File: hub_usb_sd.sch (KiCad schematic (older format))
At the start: 65 parts, among them J1 Downstream_2, J2 Downstream_3, J3 I²C, J4 Upstream, J5 SD_Card, J6 EEPROM_Pgm, J7 External_Power, U1 USB2642-I_ML, U2 TPS2052C, U3 AT24CS04BN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

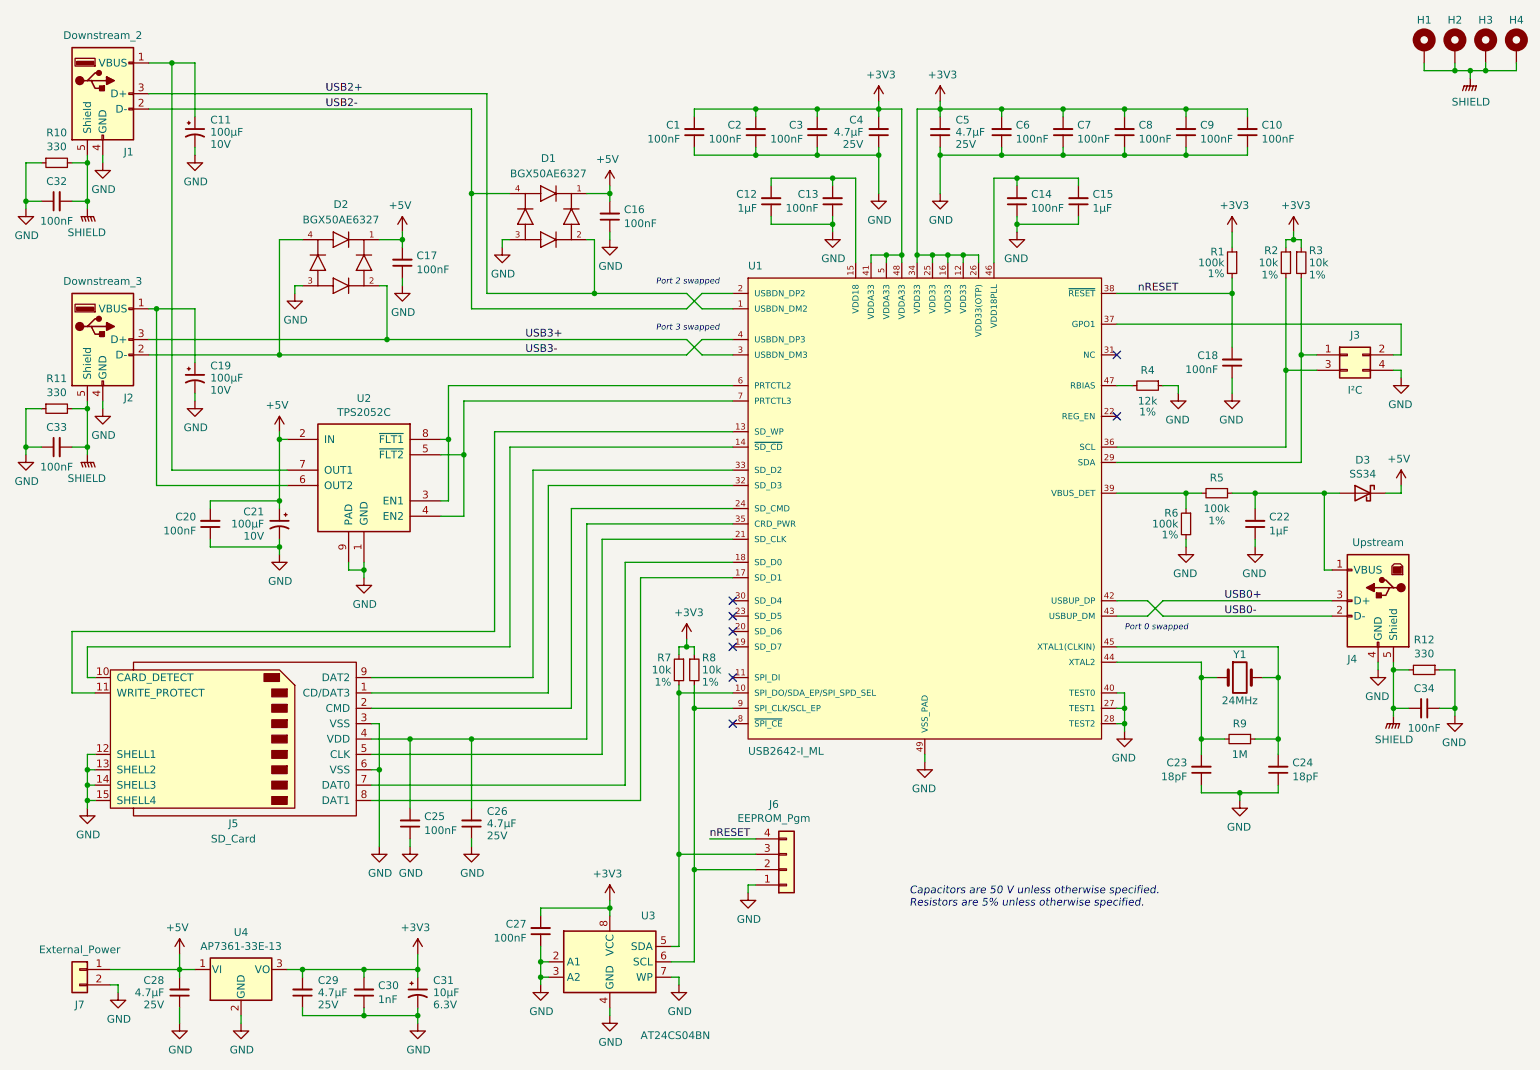
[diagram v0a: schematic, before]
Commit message: Added production remarks to schematic
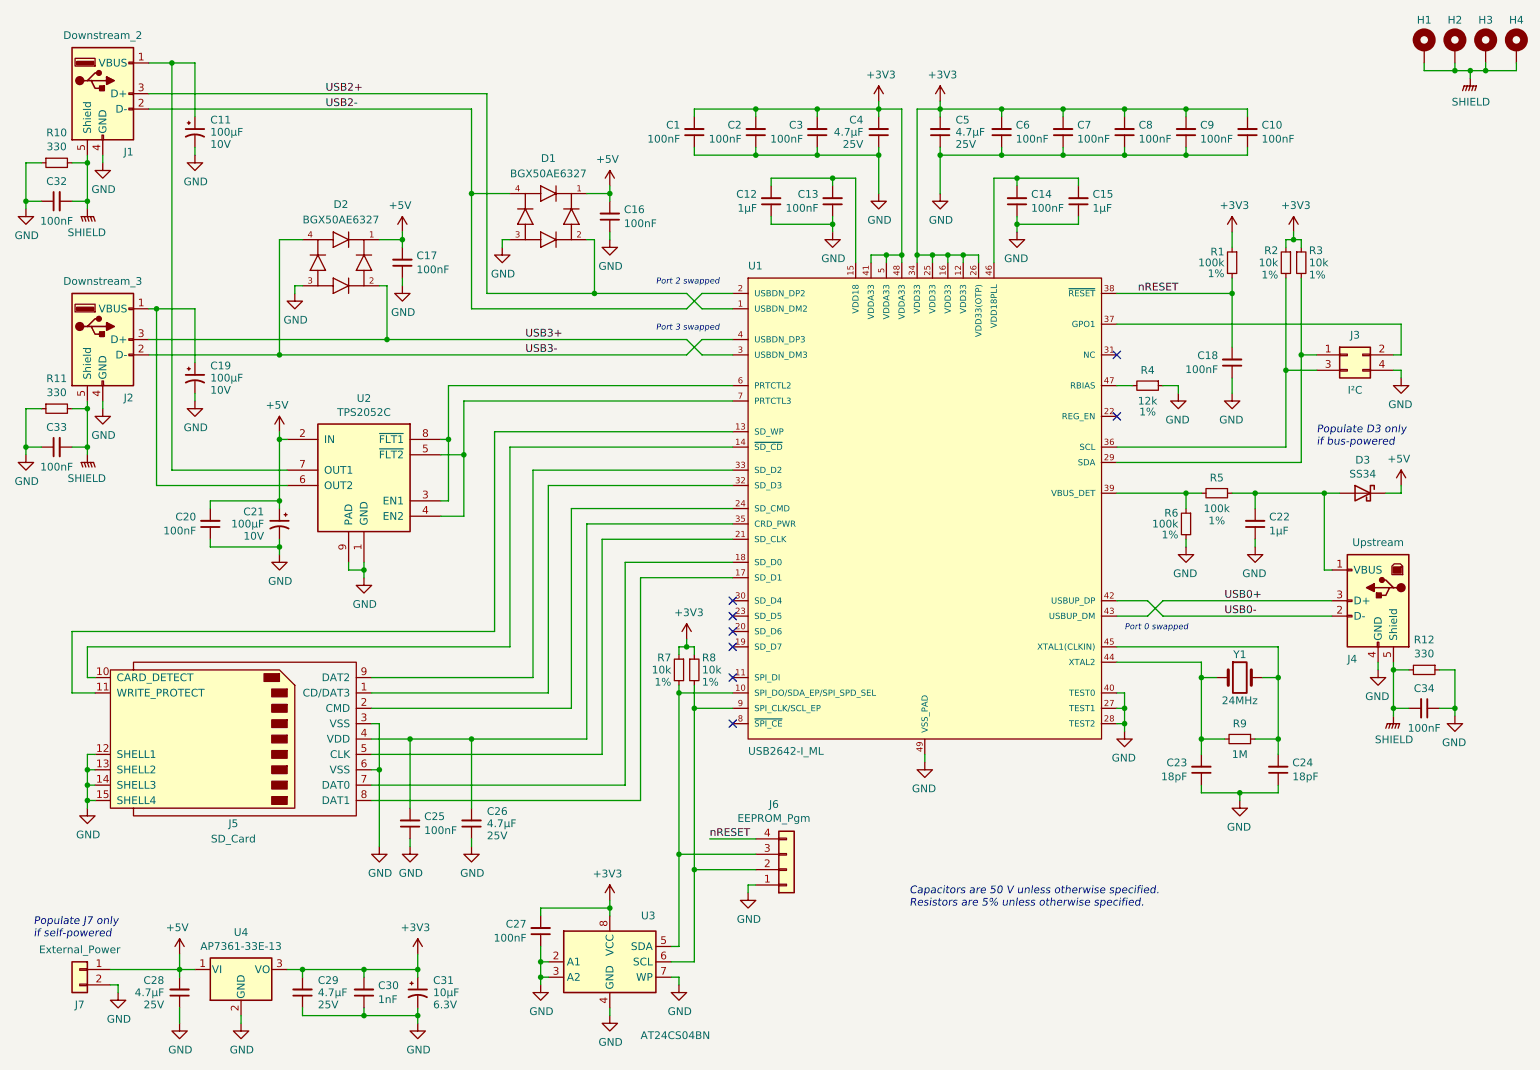
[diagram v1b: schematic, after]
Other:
- note added: "Populate D3 only\nif bus-powered"
- note added: "Populate J7 only\nif self-powered"
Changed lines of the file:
@@
 EESchema Schematic File Version 4
-LIBS:hub_usb_sd-cache
 EELAYER 30 0
 EELAYER END
@@
 	-1   0    0    -1
 $EndComp
+Text Notes 9600 3550 0    50   Italic 0
+Populate D3 only\nif bus-powered
+Text Notes 1250 6750 0    50   Italic 0
+Populate J7 only\nif self-powered
 $EndSCHEMATC

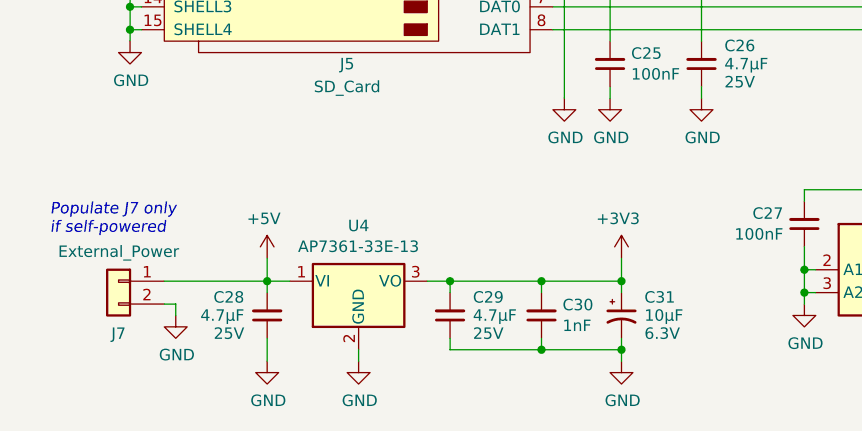
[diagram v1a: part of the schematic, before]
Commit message: Updated board layout to accommodate new power supply connector
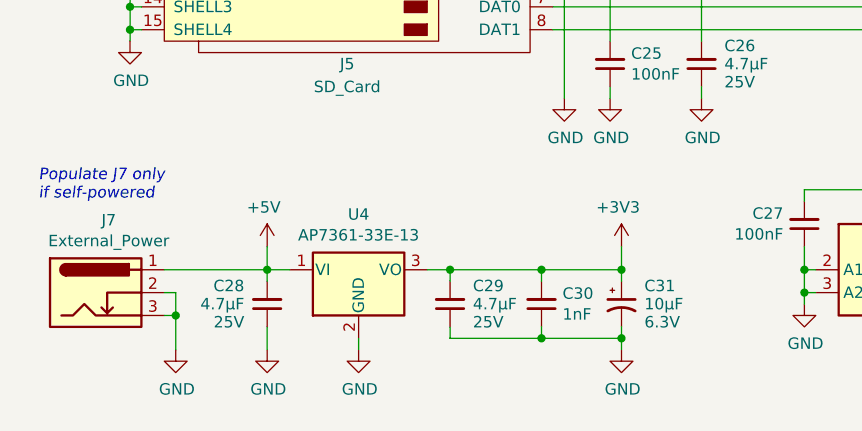
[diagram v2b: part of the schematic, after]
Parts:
- removed J7: External_Power, Extra:Metaltex_PEMN1-02_protruded_6_mm, symbol Connector_Generic:Conn_01x02
- added J7: External_Power, Extra:BarrelJack_DC-005_protruded_6_mm, symbol Connector:Barrel_Jack_Switch_Pin3Ring
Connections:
- net +5V: now also J7.1
- net GND: now also J7.2, J7.3
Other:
- moved on the sheet: C28, C29, C30, C31, U4
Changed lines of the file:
@@
 L Extra:AP7361-33E-13 U4
 U 1 1 5FBCA5FC
-P 2600 6950
-F 0 "U4" H 2600 7192 50  0000 C CNN
-F 1 "AP7361-33E-13" H 2600 7101 50  0000 C CNN
-F 2 "Package_TO_SOT_SMD:SOT-223-3_TabPin2" H 2600 7175 50  0001 C CIN
-F 3 "https://www.diodes.com/assets/Datasheets/AP7361.pdf" H 2600 6900 50  0001 C CNN
-	1    2600 6950
+P 2600 6900
+F 0 "U4" H 2600 7142 50  0000 C CNN
+F 1 "AP7361-33E-13" H 2600 7051 50  0000 C CNN
+F 2 "Package_TO_SOT_SMD:SOT-223-3_TabPin2" H 2600 7125 50  0001 C CIN
+F 3 "https://www.diodes.com/assets/Datasheets/AP7361.pdf" H 2600 6850 50  0001 C CNN
+	1    2600 6900
 	1    0    0    -1
 $EndComp
@@
 L Device:C_Small C28
 U 1 1 60440033
-P 2200 7100
-F 0 "C28" H 2100 7050 50  0000 R TNN
-F 1 "4.7µF" H 2100 7100 50  0000 R CNN
-F 2 "Capacitor_SMD:C_0805_2012Metric" H 2200 7100 50  0001 C CNN
-F 3 "~" H 2200 7100 50  0001 C CNN
-F 4 "25V" H 2100 7150 50  0000 R BNN "Voltage"
-	1    2200 7100
+P 2200 7050
+F 0 "C28" H 2100 7000 50  0000 R TNN
+F 1 "4.7µF" H 2100 7050 50  0000 R CNN
+F 2 "Capacitor_SMD:C_0805_2012Metric" H 2200 7050 50  0001 C CNN
+F 3 "~" H 2200 7050 50  0001 C CNN
+F 4 "25V" H 2100 7100 50  0000 R BNN "Voltage"
+	1    2200 7050
 	1    0    0    1
 $EndComp
@@
 L Device:C_Small C29
 U 1 1 60440A88
-P 3000 7100
-F 0 "C29" H 2900 7050 50  0000 R TNN
-F 1 "4.7µF" H 2900 7100 50  0000 R CNN
-F 2 "Capacitor_SMD:C_0805_2012Metric" H 3000 7100 50  0001 C CNN
-F 3 "~" H 3000 7100 50  0001 C CNN
-F 4 "25V" H 2900 7150 50  0000 R BNN "Voltage"
-	1    3000 7100
+P 3000 7050
+F 0 "C29" H 2900 7000 50  0000 R TNN
+F 1 "4.7µF" H 2900 7050 50  0000 R CNN
+F 2 "Capacitor_SMD:C_0805_2012Metric" H 3000 7050 50  0001 C CNN
+F 3 "~" H 3000 7050 50  0001 C CNN
+F 4 "25V" H 2900 7100 50  0000 R BNN "Voltage"
+	1    3000 7050
 	-1   0    0    1
 $EndComp
 Wire Wire Line
-	2200 7000 2200 6950
-Wire Wire Line
-	2200 6950 2300 6950
-Wire Wire Line
-	2900 6950 3000 6950
-Wire Wire Line
-	3000 6950 3000 7000
+	2200 6950 2200 6900
+Wire Wire Line
+	2200 6900 2300 6900
+Wire Wire Line
+	2900 6900 3000 6900
+Wire Wire Line
+	3000 6900 3000 6950
 $Comp
 L power:GND #PWR043
 U 1 1 605288BD
-P 1800 7100
-F 0 "#PWR043" H 1800 6850 50  0001 C CNN
-F 1 "GND" H 1805 6927 50  0000 C CNN
-F 2 "" H 1800 7100 50  0001 C CNN
-F 3 "" H 1800 7100 50  0001 C CNN
-	1    1800 7100
-	1    0    0    -1
-$EndComp
-Wire Wire Line
-	1800 7100 1800 7050
-Wire Wire Line
-	1800 7050 1750 7050
-Wire Wire Line
-	1750 6950 2200 6950
-Connection ~ 2200 6950
+P 1800 7250
+F 0 "#PWR043" H 1800 7000 50  0001 C CNN
+F 1 "GND" H 1805 7077 50  0000 C CNN
+F 2 "" H 1800 7250 50  0001 C CNN
+F 3 "" H 1800 7250 50  0001 C CNN
+	1    1800 7250
+	1    0    0    -1
+$EndComp
+Wire Wire Line
+	1800 7250 1800 7100
+Wire Wire Line
+	1800 7000 1750 7000
+Wire Wire Line
+	1750 6900 2200 6900
+Connection ~ 2200 6900
 $Comp
 L power:+5V #PWR039
 U 1 1 60587F87
-P 2200 6850
-F 0 "#PWR039" H 2200 6700 50  0001 C CNN
-F 1 "+5V" H 2215 7023 50  0000 C CNN
-F 2 "" H 2200 6850 50  0001 C CNN
-F 3 "" H 2200 6850 50  0001 C CNN
-	1    2200 6850
-	-1   0    0    -1
-$EndComp
-Wire Wire Line
-	2200 6850 2200 6950
+P 2200 6800
+F 0 "#PWR039" H 2200 6650 50  0001 C CNN
+F 1 "+5V" H 2215 6973 50  0000 C CNN
+F 2 "" H 2200 6800 50  0001 C CNN
+F 3 "" H 2200 6800 50  0001 C CNN
+	1    2200 6800
+	-1   0    0    -1
+$EndComp
+Wire Wire Line
+	2200 6800 2200 6900
 $Comp
 L power:+3V3 #PWR040
 U 1 1 605993D2
-P 3750 6850
-F 0 "#PWR040" H 3750 6700 50  0001 C CNN
-F 1 "+3V3" H 3765 7023 50  0000 C CNN
-F 2 "" H 3750 6850 50  0001 C CNN
-F 3 "" H 3750 6850 50  0001 C CNN
-	1    3750 6850
+P 3750 6800
+F 0 "#PWR040" H 3750 6650 50  0001 C CNN
+F 1 "+3V3" H 3765 6973 50  0000 C CNN
+F 2 "" H 3750 6800 50  0001 C CNN
+F 3 "" H 3750 6800 50  0001 C CNN
+	1    3750 6800
 	-1   0    0    -1
 $EndComp
@@
 L Device:C_Small C30
 U 1 1 605CA9EB
-P 3400 7100
-F 0 "C30" H 3308 7054 50  0000 R CNN
-F 1 "1nF" H 3308 7145 50  0000 R CNN
-F 2 "Capacitor_SMD:C_0603_1608Metric" H 3400 7100 50  0001 C CNN
-F 3 "~" H 3400 7100 50  0001 C CNN
-	1    3400 7100
+P 3400 7050
+F 0 "C30" H 3308 7004 50  0000 R CNN
+F 1 "1nF" H 3308 7095 50  0000 R CNN
+F 2 "Capacitor_SMD:C_0603_1608Metric" H 3400 7050 50  0001 C CNN
+F 3 "~" H 3400 7050 50  0001 C CNN
+	1    3400 7050
 	-1   0    0    1
 $EndComp
@@
 L Device:CP1_Small C31
 U 1 1 6065C2E9
-P 3750 7100
-F 0 "C31" H 3850 7150 50  0000 L BNN
-F 1 "10µF" H 3850 7100 50  0000 L CNN
-F 2 "Capacitor_Tantalum_SMD:CP_EIA-3216-18_Kemet-A" H 3750 7100 50  0001 C CNN
-F 3 "~" H 3750 7100 50  0001 C CNN
-F 4 "T491A106K006AT" H 3750 7100 50  0001 C CNN "Part#"
-F 5 "6.3V" H 3850 7050 50  0000 L TNN "Voltage"
-	1    3750 7100
-	1    0    0    -1
-$EndComp
-Wire Wire Line
-	3400 7000 3400 6950
-Wire Wire Line
-	3400 6950 3000 6950
-Connection ~ 3000 6950
-Wire Wire Line
-	3750 7000 3750 6950
-Wire Wire Line
-	3750 6950 3400 6950
-Connection ~ 3400 6950
+P 3750 7050
+F 0 "C31" H 3850 7100 50  0000 L BNN
+F 1 "10µF" H 3850 7050 50  0000 L CNN
+F 2 "Capacitor_Tantalum_SMD:CP_EIA-3216-18_Kemet-A" H 3750 7050 50  0001 C CNN
+F 3 "~" H 3750 7050 50  0001 C CNN
+F 4 "T491A106K006AT" H 3750 7050 50  0001 C CNN "Part#"
+F 5 "6.3V" H 3850 7000 50  0000 L TNN "Voltage"
+	1    3750 7050
+	1    0    0    -1
+$EndComp
+Wire Wire Line
+	3400 6950 3400 6900
+Wire Wire Line
+	3400 6900 3000 6900
+Connection ~ 3000 6900
+Wire Wire Line
+	3750 6950 3750 6900
+Wire Wire Line
+	3750 6900 3400 6900
+Connection ~ 3400 6900
 $Comp
 L power:GND #PWR047
 U 1 1 6067EFBE
-P 3750 7300
-F 0 "#PWR047" H 3750 7050 50  0001 C CNN
-F 1 "GND" H 3755 7127 50  0000 C CNN
-F 2 "" H 3750 7300 50  0001 C CNN
-F 3 "" H 3750 7300 50  0001 C CNN
-	1    3750 7300
-	1    0    0    -1
-$EndComp
-Wire Wire Line
-	3750 6850 3750 6950
-Connection ~ 3750 6950
-Wire Wire Line
-	3000 7200 3000 7250
-Wire Wire Line
-	3000 7250 3400 7250
-Wire Wire Line
-	3750 7250 3750 7300
+P 3750 7250
+F 0 "#PWR047" H 3750 7000 50  0001 C CNN
+F 1 "GND" H 3755 7077 50  0000 C CNN
+F 2 "" H 3750 7250 50  0001 C CNN
+F 3 "" H 3750 7250 50  0001 C CNN
+	1    3750 7250
+	1    0    0    -1
+$EndComp
+Wire Wire Line
+	3750 6800 3750 6900
+Connection ~ 3750 6900
+Wire Wire Line
+	3000 7150 3000 7200
+Wire Wire Line
+	3000 7200 3400 7200
 Wire Wire Line
 	3750 7200 3750 7250
-Connection ~ 3750 7250
-Wire Wire Line
-	3400 7200 3400 7250
-Connection ~ 3400 7250
-Wire Wire Line
-	3400 7250 3750 7250
+Wire Wire Line
+	3750 7150 3750 7200
+Connection ~ 3750 7200
+Wire Wire Line
+	3400 7150 3400 7200
+Connection ~ 3400 7200
+Wire Wire Line
+	3400 7200 3750 7200
 $Comp
 L power:GND #PWR046
 U 1 1 60430D3C
-P 2600 7300
-F 0 "#PWR046" H 2600 7050 50  0001 C CNN
-F 1 "GND" H 2605 7127 50  0000 C CNN
-F 2 "" H 2600 7300 50  0001 C CNN
-F 3 "" H 2600 7300 50  0001 C CNN
-	1    2600 7300
-	1    0    0    -1
-$EndComp
-Wire Wire Line
-	2600 7300 2600 7250
+P 2600 7250
+F 0 "#PWR046" H 2600 7000 50  0001 C CNN
+F 1 "GND" H 2605 7077 50  0000 C CNN
+F 2 "" H 2600 7250 50  0001 C CNN
+F 3 "" H 2600 7250 50  0001 C CNN
+	1    2600 7250
+	1    0    0    -1
+$EndComp
+Wire Wire Line
+	2600 7250 2600 7200
 $Comp
 L power:GND #PWR045
 U 1 1 60442006
-P 2200 7300
-F 0 "#PWR045" H 2200 7050 50  0001 C CNN
-F 1 "GND" H 2205 7127 50  0000 C CNN
-F 2 "" H 2200 7300 50  0001 C CNN
-F 3 "" H 2200 7300 50  0001 C CNN
-	1    2200 7300
-	1    0    0    -1
-$EndComp
-Wire Wire Line
-	2200 7300 2200 7200
+P 2200 7250
+F 0 "#PWR045" H 2200 7000 50  0001 C CNN
+F 1 "GND" H 2205 7077 50  0000 C CNN
+F 2 "" H 2200 7250 50  0001 C CNN
+F 3 "" H 2200 7250 50  0001 C CNN
+	1    2200 7250
+	1    0    0    -1
+$EndComp
+Wire Wire Line
+	2200 7250 2200 7150
 $Comp
 L Device:C_Small C26
@@
 	3550 2850 5500 2850
 $Comp
-L Connector_Generic:Conn_01x02 J7
-U 1 1 5FBF0A96
-P 1550 6950
-F 0 "J7" H 1550 6750 50  0000 C TNN
-F 1 "External_Power" H 1550 7050 50  0000 C BNN
-F 2 "Extra:Metaltex_PEMN1-02_protruded_6_mm" H 1550 6950 50  0001 C CNN
-F 3 "~" H 1550 6950 50  0001 C CNN
-F 4 "PEMN1-02" H 1550 6950 50  0001 C CNN "Part#"
-	1    1550 6950
-	-1   0    0    -1
-$EndComp
-$Comp
 L Extra:SHIELD #PWR0101
 U 1 1 5FDF8F6C
@@
 Text Notes 9600 3550 0    50   Italic 0
 Populate D3 only\nif bus-powered
-Text Notes 1250 6750 0    50   Italic 0
+$Comp
+L Connector:Barrel_Jack_Switch_Pin3Ring J7
+U 1 1 5FE1E0D9
+P 1450 7000
+F 0 "J7" H 1507 7317 50  0000 C CNN
+F 1 "External_Power" H 1507 7226 50  0000 C CNN
+F 2 "Extra:BarrelJack_DC-005_protruded_6_mm" H 1500 6960 50  0001 C CNN
+F 3 "~" H 1500 6960 50  0001 C CNN
+	1    1450 7000
+	1    0    0    -1
+$EndComp
+Wire Wire Line
+	1750 7100 1800 7100
+Connection ~ 1800 7100
+Wire Wire Line
+	1800 7100 1800 7000
+Text Notes 1200 6600 0    50   Italic 0
 Populate J7 only\nif self-powered
 $EndSCHEMATC
